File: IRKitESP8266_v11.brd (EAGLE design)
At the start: 50 x 50 mm, 34 parts, among them CN1 CON_USB-BMICRO-BN, Q1 CJ2302, U1 MOD_ESP8266WROOM02, U2 310030052_XC6228D332VR-G

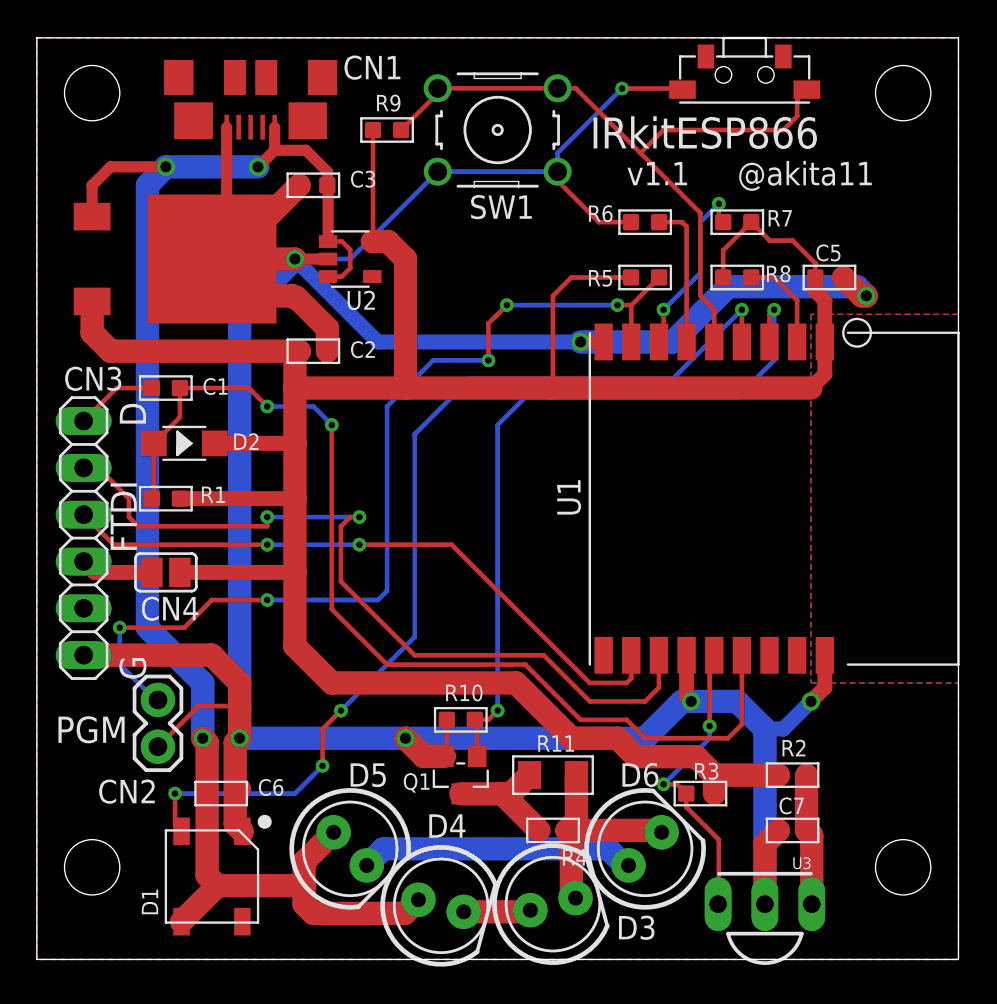
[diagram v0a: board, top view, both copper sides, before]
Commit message: ESP8266のアンテナ周囲のベタGNDの変更
設計ガイドに沿って、アンテナ周囲のベタGNDをあけ、それにともなってC5の位置を移動
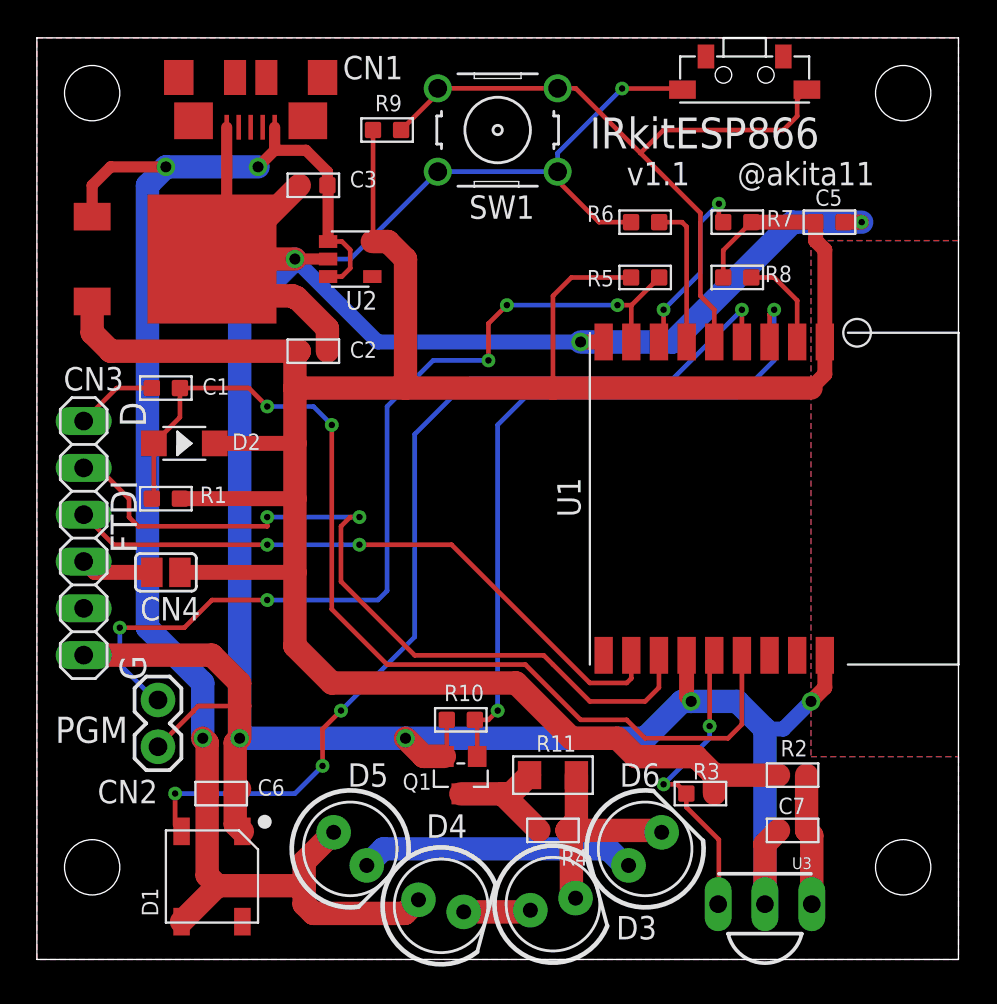
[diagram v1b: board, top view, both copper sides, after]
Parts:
- moved C5 3.00 mm to (43.0, 40.0)
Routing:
- net +3V3: track 144.6 -> 146.0 mm
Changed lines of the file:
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@@
 <element name="C1" library="Seeed-Capacitor-2016" package="C0603" value="100nf" x="7" y="31" smashed="yes" rot="R270">
 <attribute name="MPN" value="CC0603KRX7R9BB104" x="7" y="31" size="1.778" layer="27" rot="R270" display="off"/>
+<attribute name="NAME" x="8.27" y="31.254" size="0.635" layer="33" ratio="10" rot="R180"/>
 <attribute name="NAME" x="8.98" y="30.639" size="0.889" layer="25" ratio="11"/>
-<attribute name="NAME" x="8.27" y="31.254" size="0.635" layer="33" ratio="10" rot="R180"/>
 <attribute name="VALUE" x="8.27" y="32.5875" size="0.635" layer="27" ratio="10" rot="R180"/>
 </element>
 <element name="C2" library="Seeed-Capacitor-2016" package="C0603" value="2.2uf" x="15" y="33" smashed="yes" rot="R270">
 <attribute name="MPN" value="CC0603KRX7R6BB225" x="15" y="33" size="1.778" layer="27" rot="R270" display="off"/>
+<attribute name="NAME" x="16.27" y="33.254" size="0.635" layer="33" ratio="10" rot="R180"/>
 <attribute name="NAME" x="16.98" y="32.639" size="0.889" layer="25" ratio="11"/>
-<attribute name="NAME" x="16.27" y="33.254" size="0.635" layer="33" ratio="10" rot="R180"/>
 <attribute name="VALUE" x="16.27" y="34.5875" size="0.635" layer="27" ratio="10" rot="R180"/>
 </element>
 <element name="C3" library="Seeed-Capacitor-2016" package="C0603" value="2.2uf" x="15" y="42" smashed="yes" rot="R90">
 <attribute name="MPN" value="CC0603KRX7R6BB225" x="15" y="42" size="1.778" layer="27" rot="R90" display="off"/>
+<attribute name="NAME" x="13.73" y="41.746" size="0.635" layer="33" ratio="10"/>
 <attribute name="NAME" x="16.98" y="41.889" size="0.889" layer="25" ratio="11"/>
-<attribute name="NAME" x="13.73" y="41.746" size="0.635" layer="33" ratio="10"/>
 <attribute name="VALUE" x="13.73" y="40.4125" size="0.635" layer="27" ratio="10"/>
 </element>
-<element name="C5" library="Seeed-Capacitor-2016" package="C0603" value="100nf" x="43" y="37" smashed="yes" rot="R270">
-<attribute name="MPN" value="CC0603KRX7R9BB104" x="43" y="37" size="1.778" layer="27" rot="R270" display="off"/>
-<attribute name="NAME" x="42.23" y="37.889" size="0.889" layer="25" ratio="11"/>
-<attribute name="NAME" x="44.27" y="37.254" size="0.635" layer="33" ratio="10" rot="R180"/>
-<attribute name="VALUE" x="44.27" y="38.5875" size="0.635" layer="27" ratio="10" rot="R180"/>
+<element name="C5" library="Seeed-Capacitor-2016" package="C0603" value="100nf" x="43" y="40" smashed="yes" rot="R270">
+<attribute name="MPN" value="CC0603KRX7R9BB104" x="43" y="40" size="1.778" layer="27" rot="R270" display="off"/>
+<attribute name="NAME" x="44.27" y="40.254" size="0.635" layer="33" ratio="10" rot="R180"/>
+<attribute name="NAME" x="42.23" y="40.889" size="0.889" layer="25" ratio="11"/>
+<attribute name="VALUE" x="44.27" y="41.5875" size="0.635" layer="27" ratio="10" rot="R180"/>
 </element>
 <element name="C6" library="Seeed-Capacitor-2016" package="C0603" value="100nf" x="10" y="9" smashed="yes" rot="R270">
 <attribute name="MPN" value="CC0603KRX7R9BB104" x="10" y="9" size="1.778" layer="27" rot="R270" display="off"/>
+<attribute name="NAME" x="11.27" y="9.254" size="0.635" layer="33" ratio="10" rot="R180"/>
 <attribute name="NAME" x="11.98" y="8.889" size="0.889" layer="25" ratio="11"/>
-<attribute name="NAME" x="11.27" y="9.254" size="0.635" layer="33" ratio="10" rot="R180"/>
 <attribute name="VALUE" x="11.27" y="10.5875" size="0.635" layer="27" ratio="10" rot="R180"/>
 </element>
 <element name="C7" library="Seeed-Capacitor-2016" package="C0603" value="10UF 6.3V" x="41" y="7" smashed="yes" rot="R90">
 <attribute name="MPN" value="CC0603MRX5R5BB106" x="41" y="7" size="1.778" layer="27" rot="R90" display="off"/>
+<attribute name="NAME" x="39.73" y="6.746" size="0.635" layer="33" ratio="10"/>
 <attribute name="NAME" x="40.23" y="7.889" size="0.889" layer="25" ratio="11"/>
-<attribute name="NAME" x="39.73" y="6.746" size="0.635" layer="33" ratio="10"/>
 <attribute name="VALUE" x="39.73" y="5.4125" size="0.635" layer="27" ratio="10"/>
 </element>
@@
 <element name="D2" library="Seeed-Diode-2016" package="SOD-123" value="20V-1A" x="8" y="28" smashed="yes">
 <attribute name="MPN" value="B5819W" x="8" y="28" size="1.778" layer="27" display="off"/>
+<attribute name="NAME" x="7.111" y="27.365" size="0.381" layer="33" ratio="10"/>
 <attribute name="NAME" x="10.595" y="27.643" size="0.889" layer="25" ratio="11"/>
-<attribute name="NAME" x="7.111" y="27.365" size="0.381" layer="33" ratio="10"/>
 <attribute name="VALUE" x="6.095" y="25.968" size="0.889" layer="27" font="vector" ratio="11"/>
 </element>
@@
 <wire x1="40.5" y1="12.5" x2="39.5" y2="12.5" width="0.8128" layer="16"/>
 <wire x1="30.75" y1="33.5" x2="31" y2="33.75" width="0.254" layer="1"/>
-<wire x1="43.762" y1="37" x2="44.762" y2="36" width="1.27" layer="1"/>
-<wire x1="44.762" y1="36" x2="45" y2="36" width="1.27" layer="1"/>
-<via x="45" y="36" extent="1-16" drill="0.6"/>
-<wire x1="45" y1="36" x2="44.5" y2="36.5" width="1.27" layer="16"/>
-<wire x1="44.5" y1="36.5" x2="37.5" y2="36.5" width="1.27" layer="16"/>
-<wire x1="37.5" y1="36.5" x2="34.5" y2="33.5" width="1.27" layer="16"/>
 <wire x1="34.5" y1="33.5" x2="29.5" y2="33.5" width="1.27" layer="16"/>
 <wire x1="32.238" y1="40" x2="30.5" y2="40" width="0.254" layer="1"/>
@@
 <wire x1="8.5" y1="13.5" x2="8.75" y2="13.75" width="0.254" layer="1"/>
 <wire x1="8.75" y1="13.75" x2="11" y2="13.75" width="0.254" layer="1"/>
+<wire x1="43.762" y1="40" x2="44.75" y2="40" width="0.8128" layer="1"/>
+<via x="44.75" y="40" extent="1-16" drill="0.35"/>
+<wire x1="44.75" y1="40" x2="41" y2="40" width="1.27" layer="16"/>
+<wire x1="41" y1="40" x2="34.5" y2="33.5" width="1.27" layer="16"/>
 </signal>
 <signal name="+5V">
@@
 <wire x1="19.05" y1="38.95" x2="20" y2="38" width="1.27" layer="1"/>
 <wire x1="20" y1="38" x2="20" y2="31" width="1.27" layer="1"/>
-<wire x1="42.75" y1="33.5" x2="42.75" y2="31.75" width="0.8128" layer="1"/>
+<wire x1="42.75" y1="31.75" x2="42.75" y2="33.5" width="0.8128" layer="1"/>
 <wire x1="42.75" y1="31.75" x2="42" y2="31" width="0.8128" layer="1"/>
-<wire x1="42.75" y1="35.75" x2="42.75" y2="33.5" width="0.8128" layer="1"/>
-<wire x1="42.238" y1="37" x2="42.238" y2="36.262" width="0.8128" layer="1"/>
-<wire x1="42.238" y1="36.262" x2="42.75" y2="35.75" width="0.8128" layer="1"/>
 <wire x1="7.762" y1="21" x2="14" y2="21" width="0.8128" layer="1"/>
 <wire x1="9.651" y1="28" x2="14" y2="28" width="0.8128" layer="1"/>
 <wire x1="7.762" y1="25" x2="14" y2="25" width="0.8128" layer="1"/>
-<wire x1="37.238" y1="37" x2="37.238" y2="38.476" width="0.254" layer="1"/>
-<wire x1="37.238" y1="38.476" x2="38.762" y2="40" width="0.254" layer="1"/>
-<wire x1="38.762" y1="40" x2="39.762" y2="39" width="0.254" layer="1"/>
-<wire x1="41" y1="39" x2="39.762" y2="39" width="0.254" layer="1"/>
-<wire x1="42.238" y1="37" x2="42.238" y2="37.762" width="0.254" layer="1"/>
-<wire x1="42.238" y1="37.762" x2="41" y2="39" width="0.254" layer="1"/>
+<wire x1="37.238" y1="38.476" x2="37.238" y2="37" width="0.254" layer="1"/>
+<wire x1="38.762" y1="40" x2="37.238" y2="38.476" width="0.254" layer="1"/>
 <wire x1="32.238" y1="37" x2="29" y2="37" width="0.254" layer="1"/>
 <wire x1="29" y1="37" x2="28" y2="36" width="0.254" layer="1"/>
@@
 <wire x1="29" y1="12" x2="31.5" y2="12" width="1.27" layer="1"/>
 <wire x1="32.5" y1="11" x2="35.762" y2="11" width="1.27" layer="1"/>
+<wire x1="42.75" y1="38.5" x2="42.25" y2="39" width="0.8128" layer="1"/>
+<wire x1="42.25" y1="39" x2="42.25" y2="39.988" width="0.8128" layer="1"/>
+<wire x1="42.25" y1="39.988" x2="42.238" y2="40" width="0.8128" layer="1"/>
+<wire x1="42.75" y1="33.5" x2="42.75" y2="38.5" width="0.8128" layer="1"/>
+<wire x1="42.238" y1="40" x2="38.762" y2="40" width="0.8128" layer="1"/>
 </signal>
 <signal name="DTR">
@@
 <vertex x="0" y="50"/>
 <vertex x="50" y="50"/>
-<vertex x="50" y="35"/>
-<vertex x="42" y="35"/>
-<vertex x="42" y="15"/>
-<vertex x="50" y="15"/>
+<vertex x="50" y="39"/>
+<vertex x="42" y="39"/>
+<vertex x="42" y="11"/>
+<vertex x="50" y="11"/>
 <vertex x="50" y="0"/>
 <vertex x="0" y="0"/>
@@
 <vertex x="0" y="50"/>
 <vertex x="50" y="50"/>
-<vertex x="50" y="35"/>
-<vertex x="42" y="35"/>
-<vertex x="42" y="15"/>
-<vertex x="50" y="15"/>
+<vertex x="50" y="39"/>
+<vertex x="42" y="39"/>
+<vertex x="42" y="11"/>
+<vertex x="50" y="11"/>
 <vertex x="50" y="0"/>
 <vertex x="0" y="0"/>
